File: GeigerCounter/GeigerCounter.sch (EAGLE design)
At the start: 4 parts, among them IC1 OPAMP-DUALU

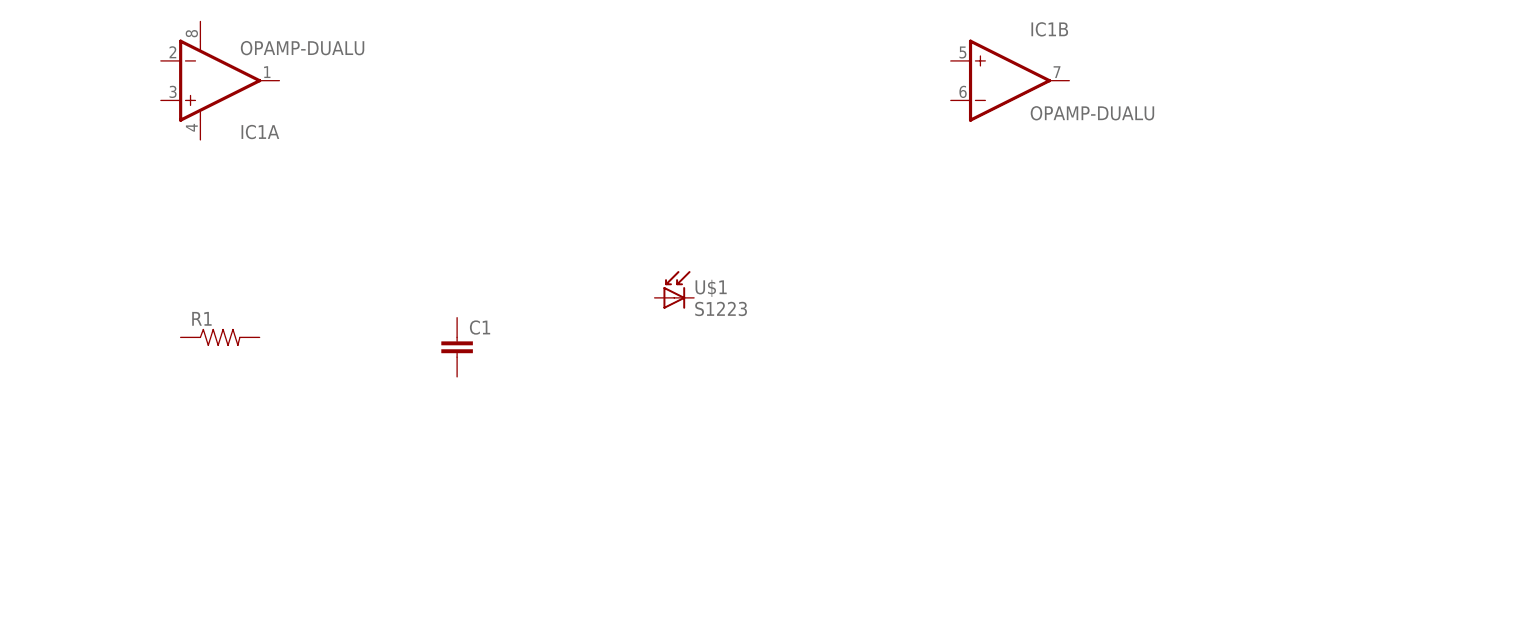
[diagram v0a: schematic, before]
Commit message: Added a new library part for the connector I will be using.
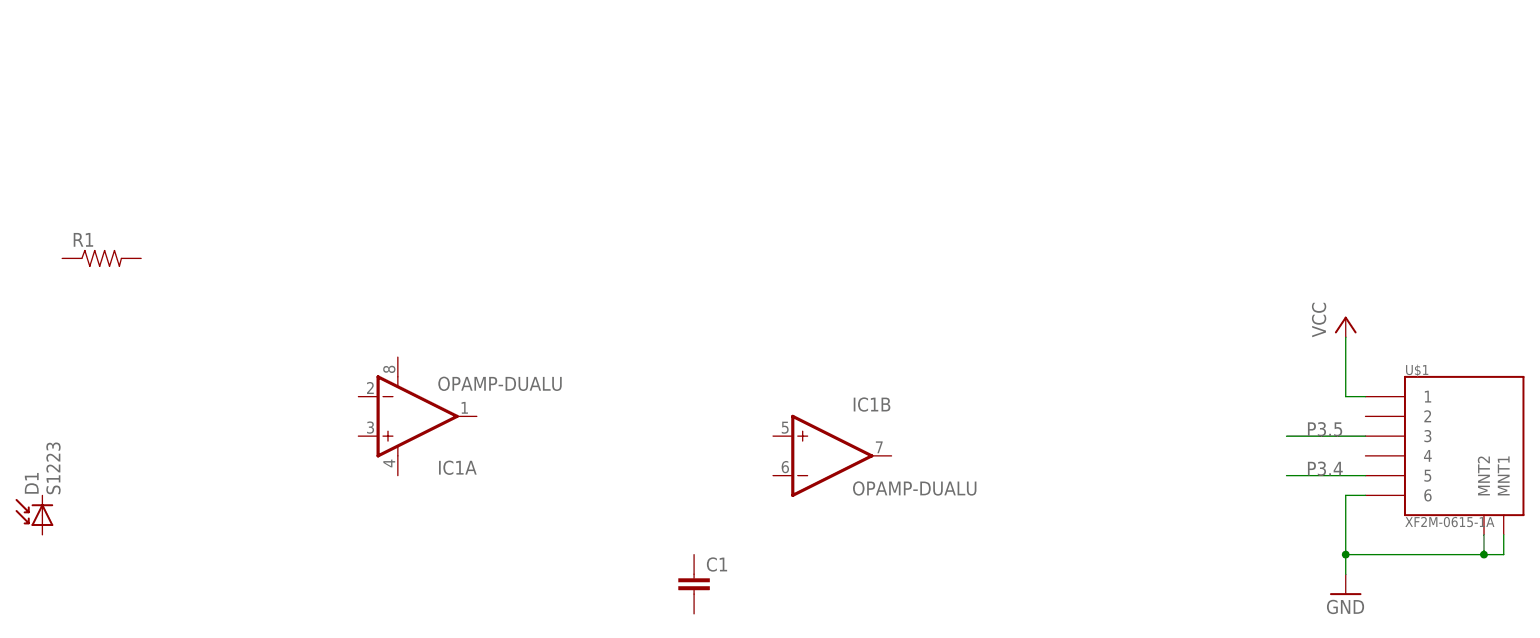
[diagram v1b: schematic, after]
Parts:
- added D1: S1223, GeigerCounter:S1223
- U$1: value S1223 -> XF2M-0615-1A; device GeigerCounter:S1223 -> GeigerCounter:XF2M-0615-1A
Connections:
- new net GND: U$1.6, U$1.MNT1, U$1.MNT2
- new net P3.4: U$1.5
- new net P3.5: U$1.3
- new net VCC: U$1.1
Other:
- moved on the sheet: C1, IC1A, IC1B, R1
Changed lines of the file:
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@@
 <part name="R1" library="SparkFun-Passives" deviceset="RESISTOR" device="AXIAL-0.3"/>
 <part name="C1" library="SparkFun-Passives" deviceset="CAP" device="PTH2"/>
-<part name="U$1" library="GeigerCounter" deviceset="S1223" device=""/>
+<part name="D1" library="GeigerCounter" deviceset="S1223" device=""/>
+<part name="GND1" library="supply1" deviceset="GND" device=""/>
+<part name="P+1" library="supply1" deviceset="VCC" device=""/>
+<part name="U$1" library="GeigerCounter" deviceset="XF2M-0615-1A" device=""/>
 </parts>
 <sheets>
@@
 </plain>
 <instances>
-<instance part="IC1" gate="A" x="35.56" y="66.04"/>
-<instance part="IC1" gate="B" x="139.7" y="66.04"/>
-<instance part="R1" gate="G$1" x="38.1" y="33.02"/>
-<instance part="C1" gate="G$1" x="68.58" y="30.48"/>
-<instance part="U$1" gate="G$1" x="96.52" y="38.1"/>
+<instance part="IC1" gate="A" x="60.96" y="22.86"/>
+<instance part="IC1" gate="B" x="116.84" y="17.78"/>
+<instance part="R1" gate="G$1" x="22.86" y="43.18"/>
+<instance part="C1" gate="G$1" x="99.06" y="0"/>
+<instance part="D1" gate="D$1" x="15.24" y="10.16" rot="R90"/>
+<instance part="GND1" gate="1" x="182.88" y="0"/>
+<instance part="P+1" gate="VCC" x="182.88" y="35.56"/>
+<instance part="U$1" gate="P$1" x="190.5" y="12.7"/>
 </instances>
 <busses>
 </busses>
 <nets>
+<net name="VCC" class="0">
+<segment>
+<pinref part="P+1" gate="VCC" pin="VCC"/>
+<wire x1="182.88" y1="33.02" x2="182.88" y2="25.4" width="0.1524" layer="91"/>
+<pinref part="U$1" gate="P$1" pin="1"/>
+<wire x1="182.88" y1="25.4" x2="185.42" y2="25.4" width="0.1524" layer="91"/>
+</segment>
+</net>
+<net name="GND" class="0">
+<segment>
+<pinref part="U$1" gate="P$1" pin="6"/>
+<wire x1="185.42" y1="12.7" x2="182.88" y2="12.7" width="0.1524" layer="91"/>
+<pinref part="GND1" gate="1" pin="GND"/>
+<wire x1="182.88" y1="12.7" x2="182.88" y2="5.08" width="0.1524" layer="91"/>
+<pinref part="U$1" gate="P$1" pin="MNT2"/>
+<wire x1="182.88" y1="5.08" x2="182.88" y2="2.54" width="0.1524" layer="91"/>
+<wire x1="182.88" y1="5.08" x2="200.66" y2="5.08" width="0.1524" layer="91"/>
+<wire x1="200.66" y1="5.08" x2="200.66" y2="7.62" width="0.1524" layer="91"/>
+<junction x="182.88" y="5.08"/>
+<pinref part="U$1" gate="P$1" pin="MNT1"/>
+<wire x1="200.66" y1="5.08" x2="203.2" y2="5.08" width="0.1524" layer="91"/>
+<wire x1="203.2" y1="5.08" x2="203.2" y2="7.62" width="0.1524" layer="91"/>
+<junction x="200.66" y="5.08"/>
+</segment>
+</net>
+<net name="P3.5" class="0">
+<segment>
+<pinref part="U$1" gate="P$1" pin="3"/>
+<wire x1="185.42" y1="20.32" x2="175.26" y2="20.32" width="0.1524" layer="91"/>
+<label x="177.8" y="20.32" size="1.778" layer="95"/>
+</segment>
+</net>
+<net name="P3.4" class="0">
+<segment>
+<pinref part="U$1" gate="P$1" pin="5"/>
+<wire x1="185.42" y1="15.24" x2="175.26" y2="15.24" width="0.1524" layer="91"/>
+<label x="177.8" y="15.24" size="1.778" layer="95"/>
+</segment>
+</net>
 </nets>
 </sheet>
